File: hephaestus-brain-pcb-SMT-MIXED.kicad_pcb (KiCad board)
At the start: 2 copper layers, 26 x 52 mm, 36 parts, among them IC1 ATSAMD51G19A-MU, J1 Barrel_Jack, J2 Conn_02x03_Odd_Even, J3 StemmaQT, J4 Conn_01x03_Female, J5 Conn_01x03_Male, J6 Conn_01x03_Male, J7 Conn_01x03_Male, J8 USB4110-GF-A, SW1 SW_SPDT, SW2 SW_SPST, SW3 SW_SPST, U1 LM1117-5.0, U2 AP2112K-3.3, U3 AT25xxx-MA, U4 74LVC1G125

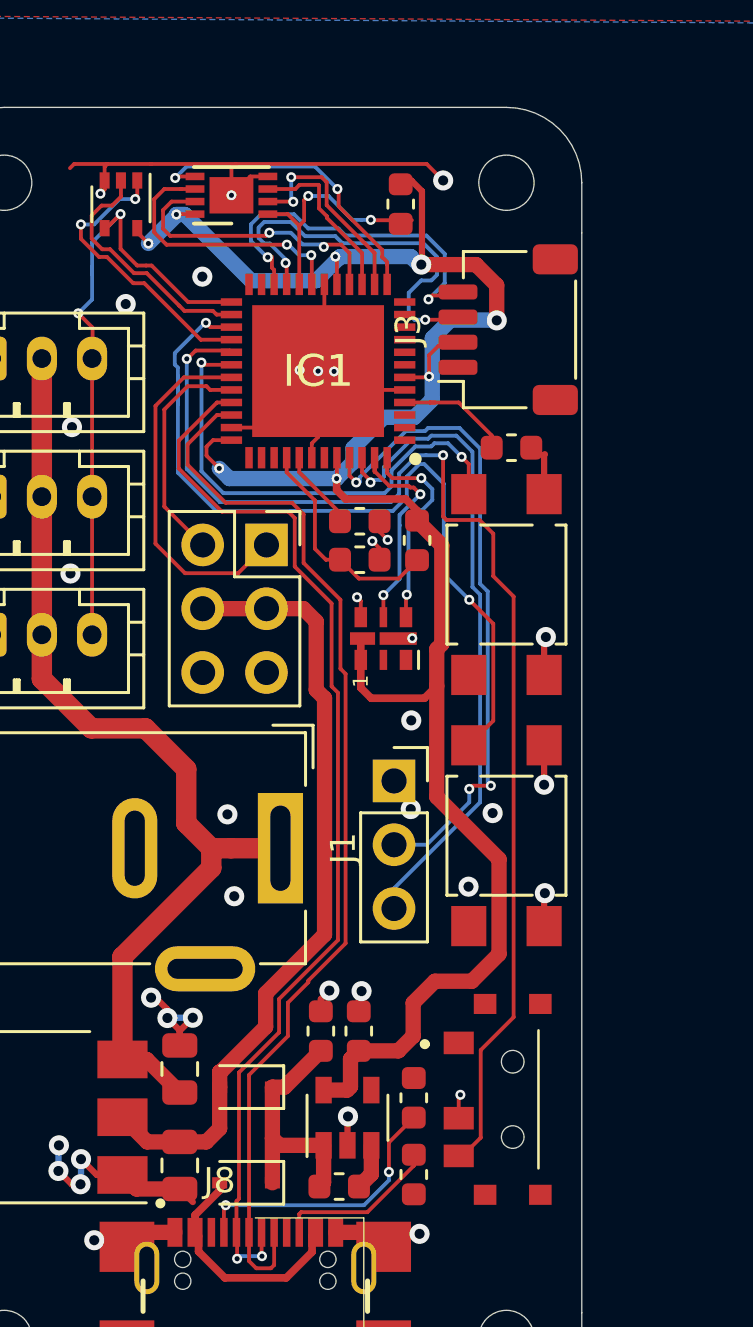
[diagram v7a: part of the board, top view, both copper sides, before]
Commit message: Switched one of the extra buttons to RESET
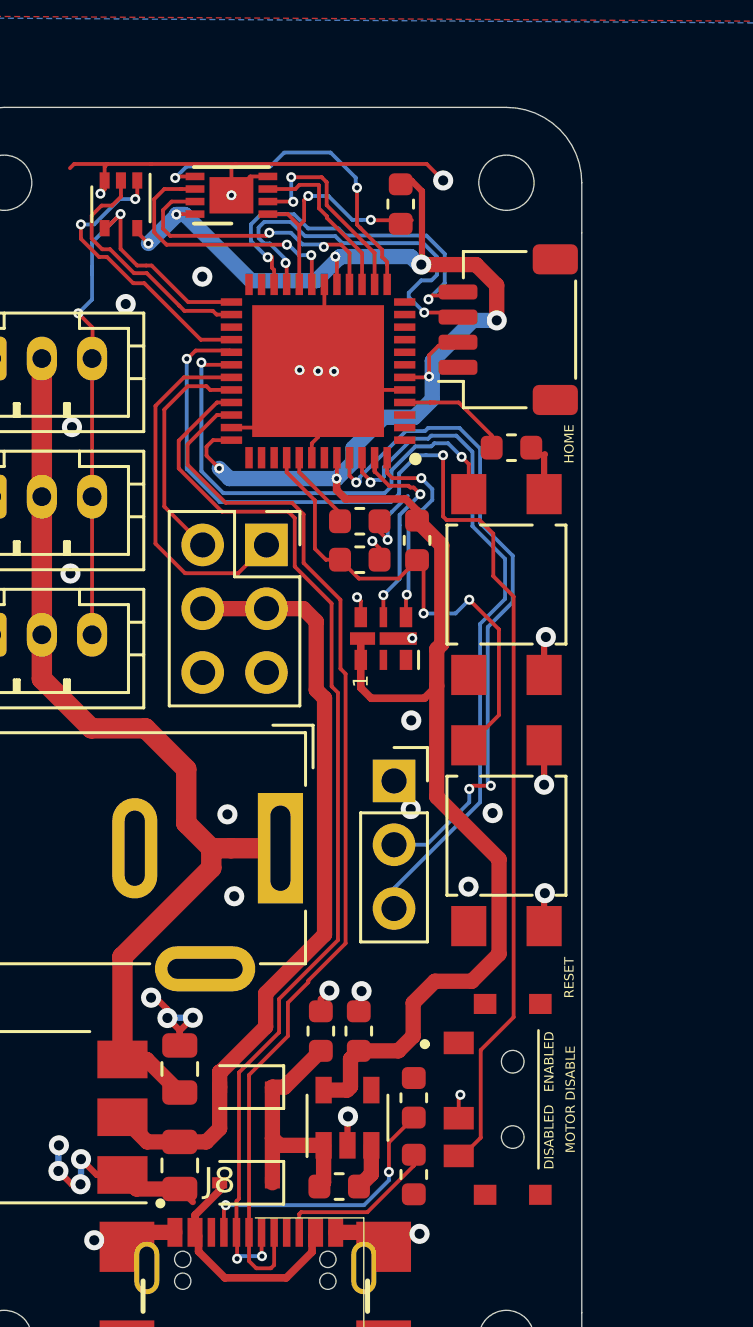
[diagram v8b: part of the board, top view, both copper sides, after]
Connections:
- C3 pad 1: Net-(C3-Pad1) -> RST
- IC1 pad 40: Net-(C3-Pad1) -> RST
- R3 pad 2: Net-(C3-Pad1) -> RST
- SW3 pad 2: 7 -> RST
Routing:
- net 7: track 33.2 -> 0.00 mm, vias 2 -> 0
- net RST: track 0.00 -> 20.0 mm, vias 0 -> 2
- net Net-(C3-Pad1): track 8.95 -> 0.00 mm
- net GND: track 66.1 -> 68.1 mm
- net QSPI_D0: track 12.5 -> 13.6 mm
- net SWCLK: track 26.1 -> 26.9 mm
- net SWDIO: track 26.1 -> 26.9 mm
- net +3V3: track 85.6 -> 85.1 mm
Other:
- board text added: "DISABLED"
- board text added: "ENABLED"
- board text added: "HOME"
- board text added: "MOTOR DISABLE"
- board text added: "RESET"
- board text added: "SWCLK"
- board text added: "SWIO"
